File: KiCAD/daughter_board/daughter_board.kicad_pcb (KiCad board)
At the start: 2 copper layers, 41 x 33 mm, 25 parts, among them IC1 QMC5883L, J1 JST, J2 S2B-PH-SM4-TB_LF__SN_2mm, U1 TPS61023DRLR, U2 SN74AHCT1G125DBVR, U3 XIAO-ESP32-C3-SMD, U4 MPU-6050

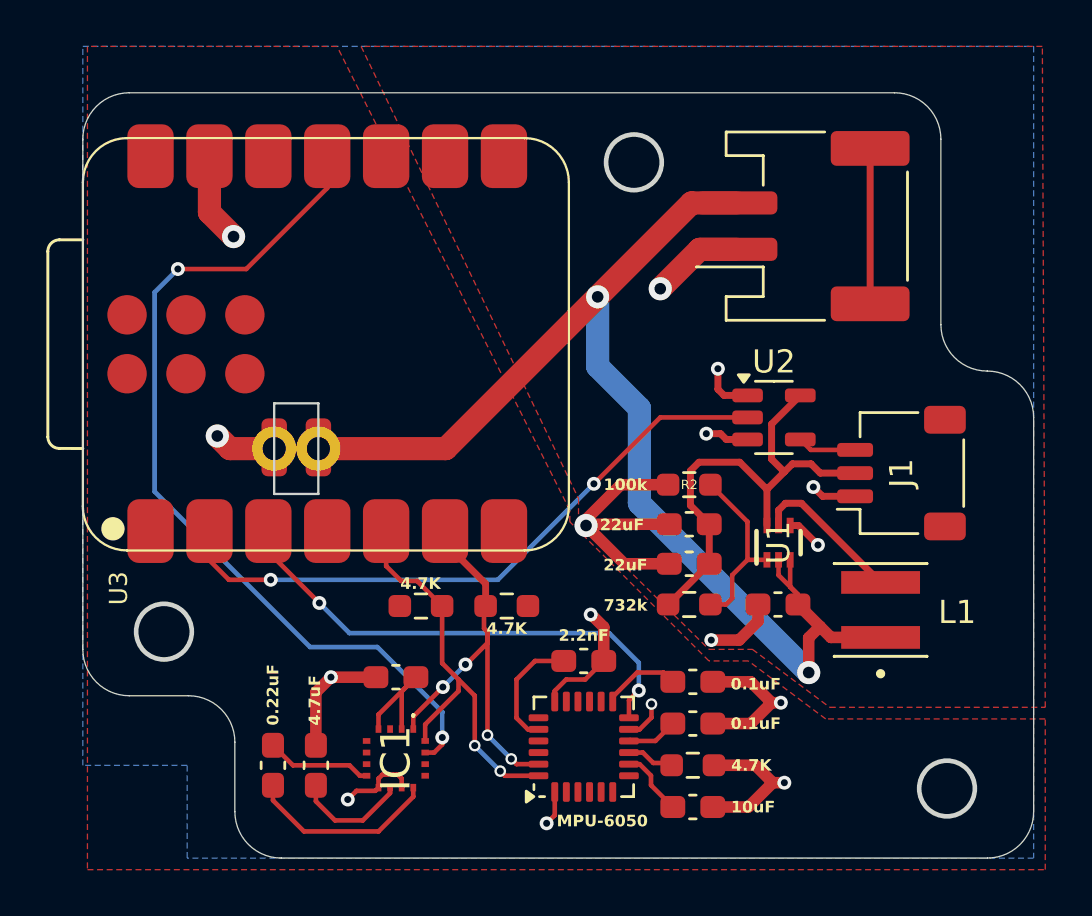
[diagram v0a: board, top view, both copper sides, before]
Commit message: in /FreeCAD model added skrews and the final daughter board,also in /Kicad added voletage divider in daughter board
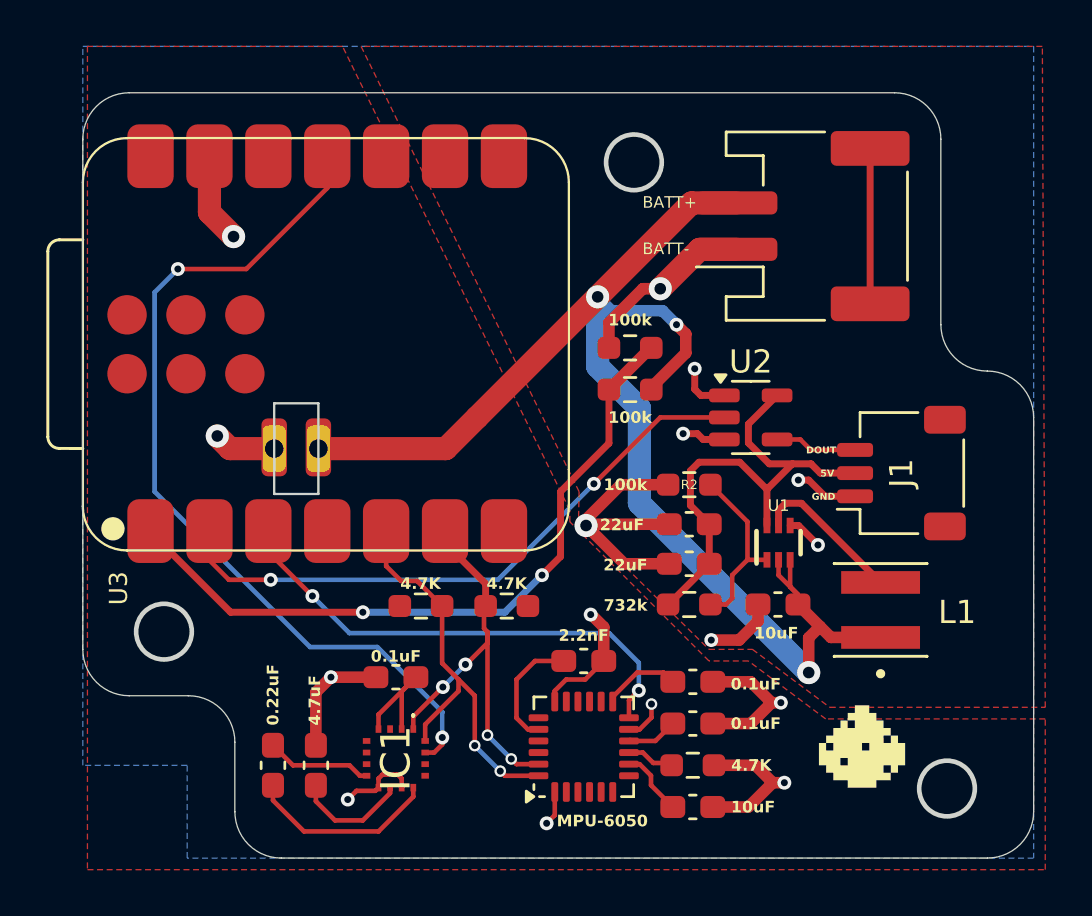
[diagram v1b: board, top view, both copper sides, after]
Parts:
- added 100k: 100k, Resistor_SMD:R_0603_1608Metric_Pad0.98x0.95mm_HandSolder, F.Cu at (106.6, 51.8)
- added 100k: 100k, Resistor_SMD:R_0603_1608Metric_Pad0.98x0.95mm_HandSolder, F.Cu at (106.6, 50.0)
- added G***: LOGO, custom_lib:red_stone_small, F.Cu at (116.6, 67.2)
- added G***: LOGO, custom_lib:red_stone, B.Cu at (96.4, 46.4)
- moved U2 1.00 mm to (111.8, 53.0)
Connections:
- U3 pad 1: unconnected-(U3-GPIO2_A0_D0-Pad1) -> /ADC
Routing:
- net /ADC: track 0.00 -> 30.8 mm, vias 0 -> 2
- net +BATT: track 52.6 -> 60.1 mm, vias 2 -> 3
- net -BATT: track 63.4 -> 68.1 mm
- net /ESP_DOUT: track 27.7 -> 26.7 mm
- net /DOUT: track 2.55 -> 3.55 mm
- net /5V: track 20.8 -> 21.6 mm

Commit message: in /KiCAD changed the silkscreen from actual values to reference notations
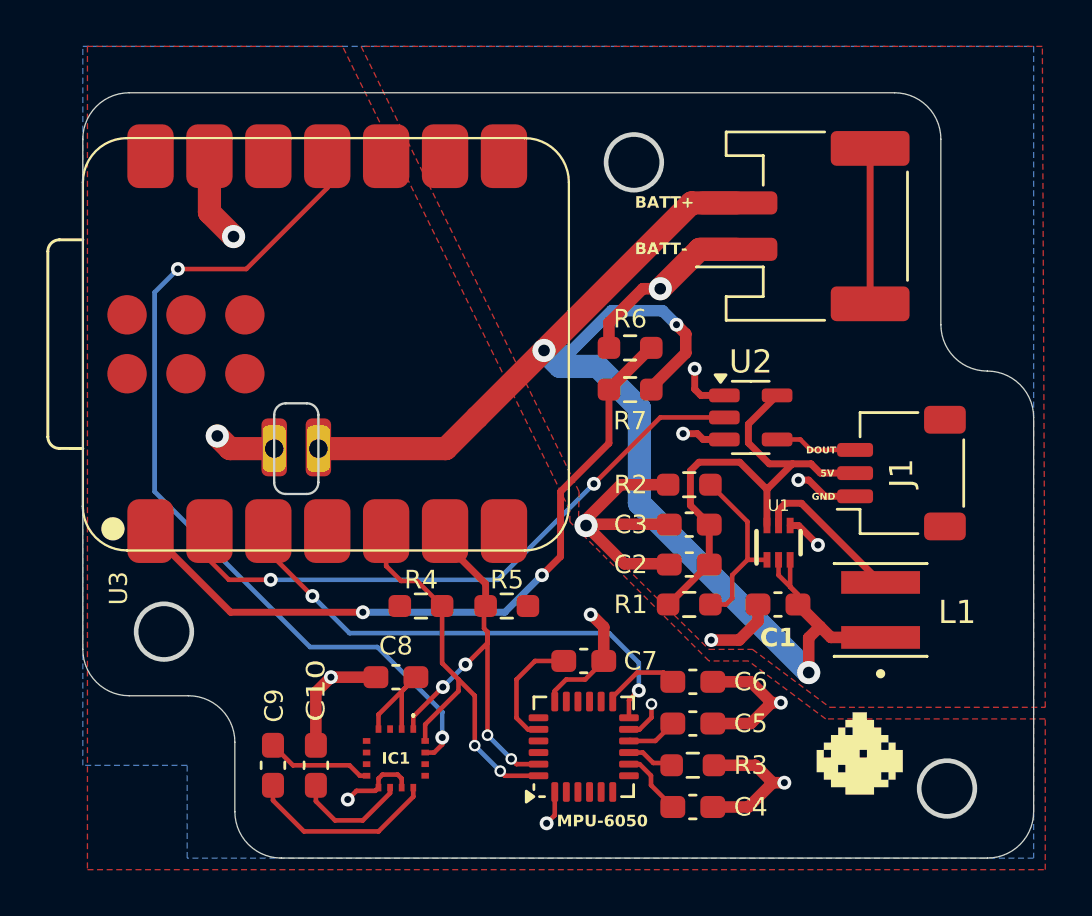
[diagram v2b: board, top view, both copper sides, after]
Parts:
- moved G*** 0.32 mm to (116.5, 67.5)
- renumbered 100k to R6, 100k to R7
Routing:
- net +BATT: track 60.1 -> 62.5 mm
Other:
- outline, holes or cut-outs redrawn
